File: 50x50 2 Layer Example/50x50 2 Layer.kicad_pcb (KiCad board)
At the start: 2 copper layers, 50 x 50 mm, 76 parts, among them J1 Conn_01x02, J2 Conn_01x02, J3 USB_C_Receptacle_USB2.0_14P, J4 Conn_01x03, J5 Conn_01x04, SW1 SW_SPST, SW2 Reset, U1 RP2040, U2 W25Q128JVPIQ TR, U3 Voltage Regulator, Y1 12MHz

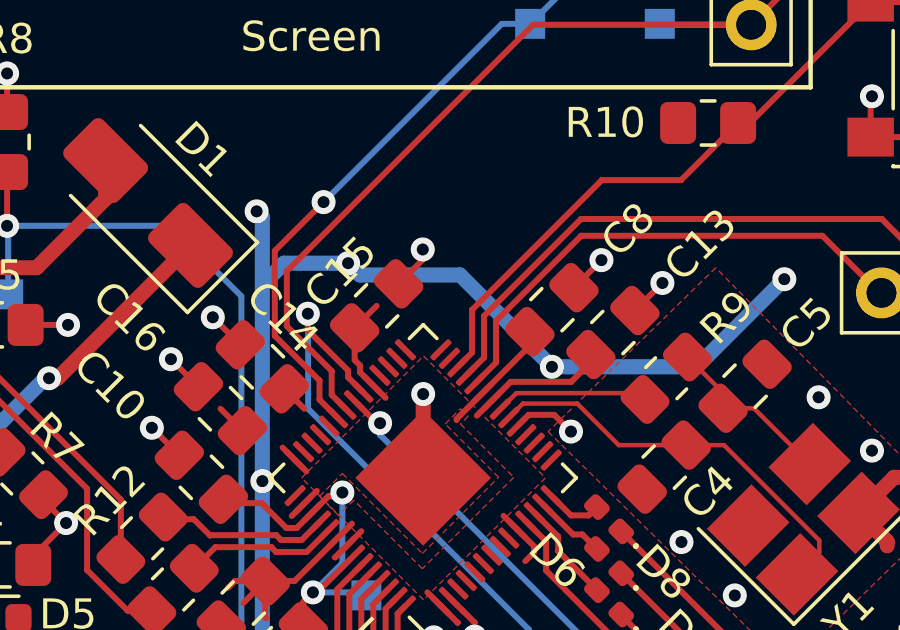
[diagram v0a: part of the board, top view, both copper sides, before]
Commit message: Rework power input switching and protection
- Replace diode-OR with DPDT source select (VBUS/battery) plus
  separate on/off switch
- Add SMAJ8.5A TVS on the battery input
- Add per-source indicator LEDs, 820R battery / 560R USB
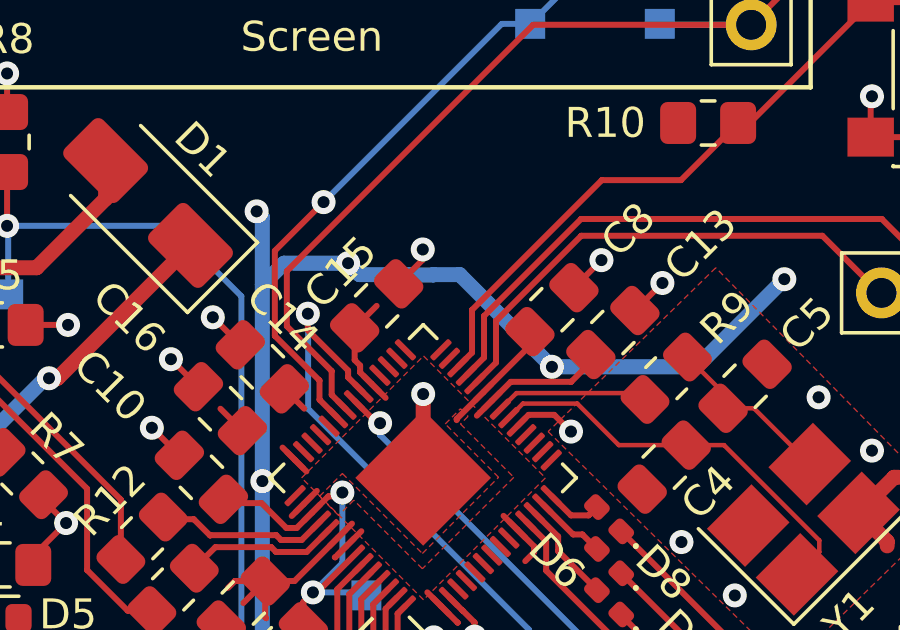
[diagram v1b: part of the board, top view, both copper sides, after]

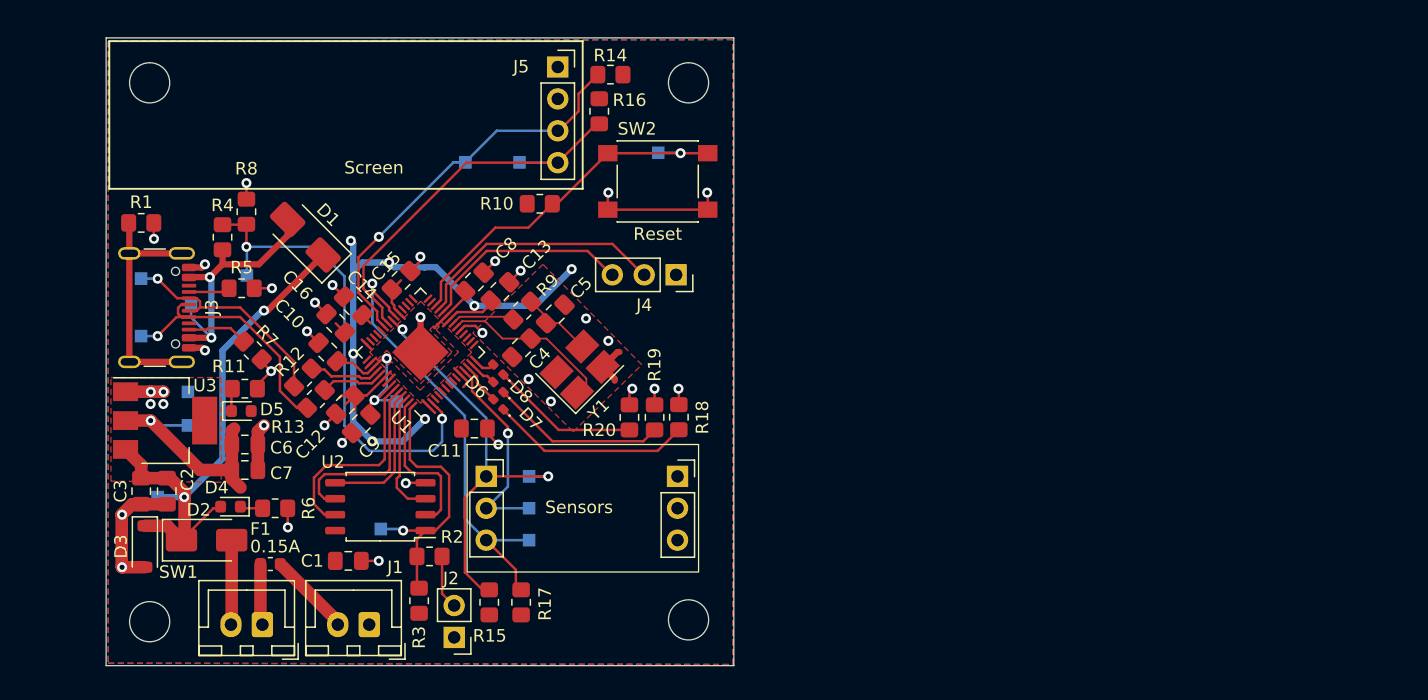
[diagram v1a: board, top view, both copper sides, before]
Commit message: Added Footprint for new Switches Attached LCSC numbers to components Started Cost Optimisation
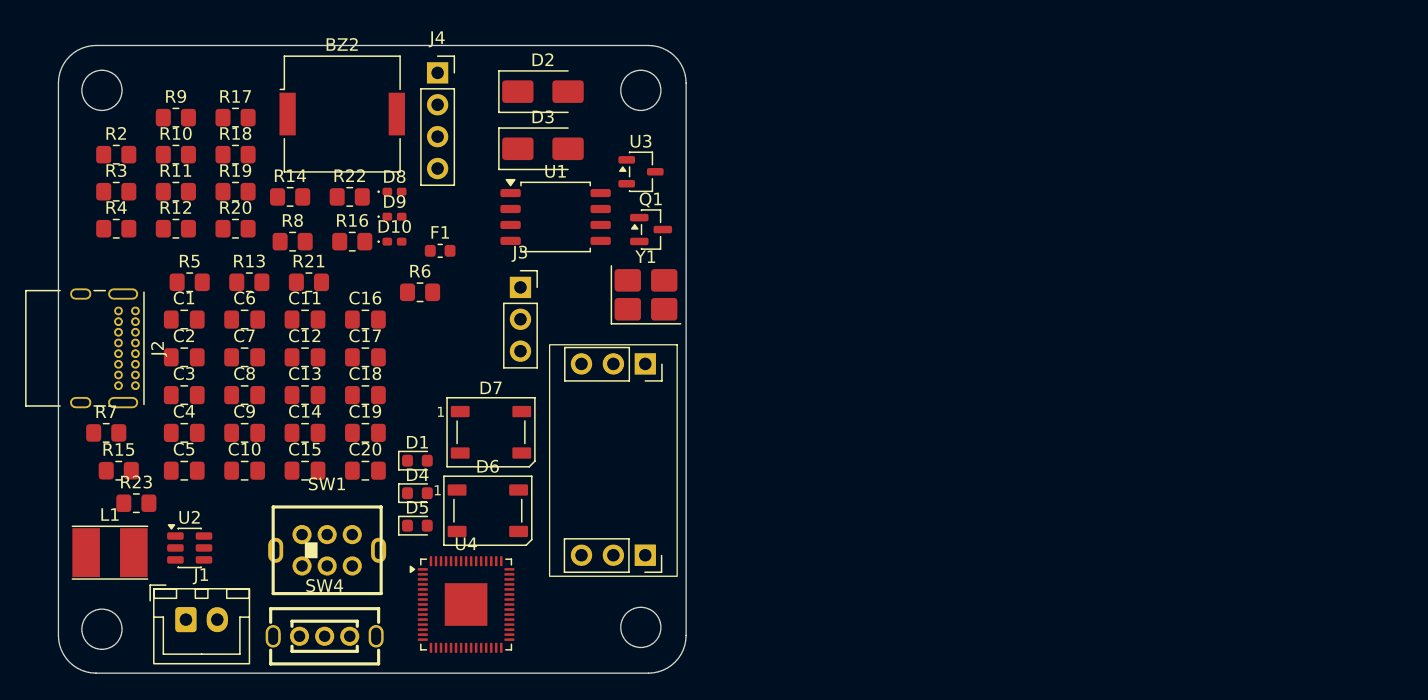
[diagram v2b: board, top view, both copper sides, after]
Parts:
- removed J5: Conn_01x04, Connector_PinSocket_2.54mm:PinSocket_1x04_P2.54mm_Vertical
- removed R1: 0R, Resistor_SMD:R_0805_2012Metric_Pad1.20x1.40mm_HandSolder
- removed SW2: Reset, Button_Switch_SMD:SW_SPST_PTS645
- removed TP1: GND, TestPoint:TestPoint_Pad_1.0x1.0mm
- removed TP10: 1V1, TestPoint:TestPoint_Pad_1.0x1.0mm
- removed TP11: INT_1, TestPoint:TestPoint_Pad_1.0x1.0mm
- removed TP12: I2C0_SCL, TestPoint:TestPoint_Pad_1.0x1.0mm
- removed TP13: I2C1_SCL, TestPoint:TestPoint_Pad_1.0x1.0mm
- removed TP14: I2C0_SDA, TestPoint:TestPoint_Pad_1.0x1.0mm
- removed TP15: I2C1_SDA, TestPoint:TestPoint_Pad_1.0x1.0mm
- removed TP2: VBUS, TestPoint:TestPoint_Pad_1.0x1.0mm
- removed TP3: D-, TestPoint:TestPoint_Pad_1.0x1.0mm
- removed TP4: D+, TestPoint:TestPoint_Pad_1.0x1.0mm
- removed TP5: USB_BOOT, TestPoint:TestPoint_Pad_1.0x1.0mm
- removed TP6: USB_DET, TestPoint:TestPoint_Pad_1.0x1.0mm
- removed TP7: BATT, TestPoint:TestPoint_Pad_1.0x1.0mm
- removed TP8: 3V3, TestPoint:TestPoint_Pad_1.0x1.0mm
- removed TP9: RST, TestPoint:TestPoint_Pad_1.0x1.0mm
- added BZ2: Buzzer, Buzzer_Beeper:Buzzer_Murata_PKMCS0909E, F.Cu at (97.0, 43.4)
- added C17: 100n, Capacitor_SMD:C_0805_2012Metric_Pad1.18x1.45mm_HandSolder, F.Cu at (98.8, 62.8)
- added C18: 100n, Capacitor_SMD:C_0805_2012Metric_Pad1.18x1.45mm_HandSolder, F.Cu at (98.8, 65.8)
- added C19: 100n, Capacitor_SMD:C_0805_2012Metric_Pad1.18x1.45mm_HandSolder, F.Cu at (98.8, 68.8)
- added C20: 10u, Capacitor_SMD:C_0805_2012Metric_Pad1.18x1.45mm_HandSolder, F.Cu at (98.8, 71.8)
- added D10: LED, LED_SMD:LED_0402_1005Metric_Pad0.77x0.64mm_HandSolder, F.Cu at (101.2, 53.6)
- added D9: LED, LED_SMD:LED_0402_1005Metric_Pad0.77x0.64mm_HandSolder, F.Cu at (101.2, 51.6)
- added L1: 3.3u, Inductor_SMD:L_Taiyo-Yuden_NR-40xx_HandSoldering, F.Cu at (78.5, 78.3)
- added Q1: MMBT3904, Package_TO_SOT_SMD:SOT-23, F.Cu at (121.6, 52.6)
- added R21: 80, Resistor_SMD:R_0805_2012Metric_Pad1.20x1.40mm_HandSolder, F.Cu at (94.3, 56.8)
- added R22: 80, Resistor_SMD:R_0805_2012Metric_Pad1.20x1.40mm_HandSolder, F.Cu at (97.6, 50.0)
- added R23: 80, Resistor_SMD:R_0805_2012Metric_Pad1.20x1.40mm_HandSolder, F.Cu at (80.6, 74.4)
- added SW4: ON_SW, Footprints:SW-TH_3P-L8.6-W4.5-P2.60, F.Cu at (95.6, 85.0)
- added U5: Sensor Board, Footprints:UCA_Sense, F.Cu at (118.6, 71.0)
- C1, C14, C15, C9: value 100nF -> 100n
- C10, C16: value 1uF -> 100n
- C11, C12, C13: value 100nF -> 4.7u
- C2: value 10uF -> 1u
- C3, C6: value 100nF -> 22u
- C4, C5: value 20pF -> 100n
- C7: value 10uF -> 15p
- C8: value 100nF -> 15p
- D1: value D_Schottky -> Blue LED; footprint Diode_SMD:D_SMA -> LED_SMD:LED_0603_1608Metric
- D3: value D_Zener -> SMAJ8.5A; footprint Diode_SMD:D_SOD-123 -> Diode_SMD:D_SMA
- D4: value Orange LED -> Green LED
- D6, D7: value LED -> WS2812B; footprint LED_SMD:LED_0402_1005Metric_Pad0.77x0.64mm_HandSolder -> LED_SMD:LED_WS2812B_PLCC4_5.0x5.0mm_P3.2mm
- F1: value 0.15A -> 0.25A
- J2: value Conn_01x02 -> USB_C_Receptacle_USB2.0_14P; footprint Connector_PinHeader_2.54mm:PinHeader_1x02_P2.54mm_Vertical -> Connector_USB:USB_C_Receptacle_GCT_USB4085
- J3: value USB_C_Receptacle_USB2.0_14P -> Conn_01x03; footprint Connector_USB:USB_C_Receptacle_GCT_USB4105-xx-A_16P_TopMnt_Horizontal -> Connector_PinSocket_2.54mm:PinSocket_1x03_P2.54mm_Vertical
- J4: value Conn_01x03 -> Conn_01x04; footprint Connector_PinSocket_2.54mm:PinSocket_1x03_P2.54mm_Vertical -> Connector_PinSocket_2.54mm:PinSocket_1x04_P2.54mm_Vertical
- R10: value 10k -> 1k
- R11: value 360R -> 360
- R12: value 27.4 -> 33
- R13: value 27.4 -> 27
- R14: value 4K7 -> 27
- R15, R16: value 4K7 -> 1k
- R18, R19, R20: value 130 -> 4K7
- R2: value 1k -> 820
- R3: value DNP -> 5k1
- R4: value 5.6k -> 560
- R5: value 5.1k -> 5k6
- R6: value 470R -> 5k1
- R7: value 5.1k -> 10k
- SW1: value SW_SPST -> PWR_SELECT; footprint Connector_JST:JST_XH_B2B-XH-A_1x02_P2.50mm_Vertical -> Footprints:SW-TH_KH-SS22D07-VG4H
- U1: value RP2040 -> W25Q32JVSSIQ; footprint Package_DFN_QFN:QFN-56-1EP_7x7mm_P0.4mm_EP3.2x3.2mm -> Package_SO:SOIC-8_5.3x5.3mm_P1.27mm
- U2: value W25Q128JVPIQ TR -> USBLC6-2SC6; footprint Package_SO:SOIC-8_5.23x5.23mm_P1.27mm -> Package_TO_SOT_SMD:SOT-23-6
- U3: value Voltage Regulator -> Voltage Regulator (MCP1755S-3302E/DB); footprint Package_TO_SOT_SMD:SOT-223 -> Package_TO_SOT_SMD:SOT-23-3
- U4: value ~ -> RP2354A; footprint Sense Board:UCA_Sense -> Package_DFN_QFN:QFN-60-1EP_7x7mm_P0.4mm_EP3.4x3.4mm
- moved D3 44.8 mm to (113.0, 46.2), turned to 0 degrees
- moved R17 44.8 mm to (88.5, 43.7), turned to 0 degrees
- moved D2 44.7 mm to (113.0, 41.6)
- moved U3 42.8 mm to (120.8, 48.0)
- moved R18 41.0 mm to (88.5, 46.6), turned to 0 degrees
- moved R2 40.6 mm to (79.0, 46.6), turned to 0 degrees
- moved R3 40.5 mm to (79.0, 49.6), turned to 0 degrees
- moved R19 37.9 mm to (88.5, 49.6), turned to 0 degrees
- moved J2 36.3 mm to (80.5, 59.1), turned to -90 degrees
- moved R20 34.8 mm to (88.5, 52.5), turned to 0 degrees
- moved C5 32.1 mm to (84.4, 71.8), turned to 0 degrees
- moved R9 31.6 mm to (83.8, 43.7), turned to 0 degrees
- moved R15 31.3 mm to (79.2, 71.8), turned to 0 degrees
- moved J3 30.1 mm to (111.2, 57.2), turned to 0 degrees
- moved R10 29.3 mm to (83.8, 46.6), turned to 0 degrees
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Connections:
- C1 pad 1: GND -> +3V3
- C1 pad 2: +3V3 -> GND
- C10 pad 1: GND -> +3V3
- C10 pad 2: +1V1 -> GND
- C11 pad 1: +3V3 -> GND
- C11 pad 2: GND -> +3V3
- C12 pad 1: +3V3 -> GND
- C12 pad 2: GND -> +1V1
- C13 pad 1: +3V3 -> GND
- C13 pad 2: GND -> Net-(U4-VREG_AVDD)
- C15 pad 1: GND -> +3V3
- C15 pad 2: +3V3 -> GND
- C16 pad 1: GND -> +3V3
- C16 pad 2: +3V3 -> GND
- C2 pad 1: +BATT -> +3V3
- C3 pad 1: +BATT -> VOUT
- C4 pad 1: /XIN -> VOUT
- C5 pad 1: Net-(C5-Pad1) -> +3V3
- C7 pad 1: +3V3 -> /XIN
- C8 pad 1: +1V1 -> Net-(C8-Pad1)
- C9 pad 1: +1V1 -> +3V3
- D1 pad 1: +BATT -> Net-(D1-K)
- D1 pad 2: VBUS -> Net-(D1-A)
- D2 pad 1: +BATT -> Net-(D2-K)
- D3 pad 1: +BATT -> Net-(D2-K)
- D4 pad 2: +BATT -> Net-(D4-A)
- D6 pad 1: Net-(D6-K) -> +3V3
- D6 pad 2: /LED_RED -> Net-(D6-DOUT)
- D7 pad 1: Net-(D7-K) -> +3V3
- D7 pad 2: /LED_YELLOW -> unconnected-(D7-DOUT-Pad2)
- D8 pad 2: /LED_GREEN -> /LED_RED
- F1 pad 1: Net-(SW1-A) -> Net-(D2-A)
- J4 pad 2: /SWD -> +3V3
- J4 pad 3: /SWCLK -> /I2C0_SCL
- R10 pad 1: /RUN -> Net-(R10-Pad1)
- R10 pad 2: +3V3 -> GND
- R12 pad 1: D- -> +3V3
- R12 pad 2: /USB_D- -> Net-(U4-VREG_AVDD)
- R13 pad 1: D+ -> D-
- R13 pad 2: /USB_D+ -> /USB_D-
- R14 pad 1: I2C0_SCL -> D+
- R14 pad 2: +3V3 -> /USB_D+
- R15 pad 1: I2C1_SCL -> Net-(Q1-B)
- R15 pad 2: +3V3 -> /BUZZER
- R16 pad 1: I2C0_SDA -> +3V3
- R16 pad 2: +3V3 -> Net-(BZ2--)
- R17 pad 1: I2C1_SDA -> /I2C0_SCL
- R18 pad 1: Net-(D6-K) -> /I2C1_SCL
- R18 pad 2: GND -> +3V3
- R19 pad 1: Net-(D7-K) -> /I2C0_SDA
- R19 pad 2: GND -> +3V3
- R2 pad 1: Net-(J2-Pin_2) -> Net-(D1-K)
- R2 pad 2: /QSPI_SS -> GND
- R20 pad 1: Net-(D8-K) -> /I2C1_SDA
- R20 pad 2: GND -> +3V3
- R3 pad 1: +3V3 -> Net-(J2-CC1)
- R3 pad 2: /QSPI_SS -> GND
- R4 pad 1: VBUS -> Net-(D4-K)
- R4 pad 2: USB_DET -> GND
- R5 pad 1: Net-(J3-CC1) -> VBUS
- R5 pad 2: GND -> USB_DET
- R6 pad 1: Net-(D4-K) -> GND
- R6 pad 2: GND -> Net-(J2-CC2)
- R7 pad 1: GND -> /SPI1_CSn
- R7 pad 2: Net-(J3-CC2) -> +3V3
- R9 pad 1: /Xout -> /XOUT
- R9 pad 2: Net-(C5-Pad1) -> Net-(C8-Pad1)
- SW1 pad 1: Net-(SW1-A) -> Net-(D2-K)
- SW1 pad 2: Net-(D2-A) -> Net-(SW1A-B)
- U1 pad 1: +3V3 -> /SPI1_CSn
- U1 pad 2: USB_DET -> /SPI1_MISO
- U1 pad 3: /GPIO_1 -> +3V3
- U1 pad 4: /GPIO_2 -> GND
- U1 pad 5: /GPIO_3 -> /SPI1_MOSI
- U1 pad 6: /GPIO_4 -> /SPI1_SCK
- U1 pad 7: /GPIO_5 -> +3V3
- U1 pad 8: /GPIO_6 -> +3V3
- U2 pad 1: /QSPI_SS -> Net-(J2-D--PadA7)
- U2 pad 2: /QSPI_SD1 -> GND
- U2 pad 3: /QSPI_SD2 -> Net-(J2-D+-PadA6)
- U2 pad 4: GND -> D+
- U2 pad 5: /QSPI_SD0 -> VBUS
- U2 pad 6: /QSPI_SCLK -> D-
- U3 pad 3: +BATT -> VOUT
- U4 pad 1: I2C1_SCL -> +3V3
- U4 pad 2: INT_1 -> USB_DET
- U4 pad 3: I2C1_SDA -> /LED_RGB
- U4 pad 4: GND -> /BUZZER
- U4 pad 5: unconnected-(U4-Pad5) -> /GPIO_3
- Y1 pad 3: Net-(C5-Pad1) -> Net-(C8-Pad1)
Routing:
- net +3V3: track 85.1 -> 0.00 mm, vias 8 -> 0
- net GND: track 66.6 -> 0.00 mm, vias 36 -> 0
- net +BATT: track 44.5 -> 0.00 mm, vias 2 -> 0
- net USB_DET: track 39.1 -> 0.00 mm, vias 2 -> 0
- net I2C1_SDA: track 36.1 -> 0.00 mm, vias 1 -> 0
- net I2C1_SCL: track 32.6 -> 0.00 mm, vias 2 -> 0
- net I2C0_SCL: track 32.3 -> 0.00 mm, vias 1 -> 0
- net I2C0_SDA: track 31.9 -> 0.00 mm
- net /RUN: track 29.4 -> 0.00 mm, vias 1 -> 0
- net /QSPI_SS: track 22.2 -> 0.00 mm, vias 1 -> 0
- net VBUS: track 21.5 -> 0.00 mm, vias 2 -> 0
- net D+: track 21.2 -> 0.00 mm, vias 1 -> 0
- net /SWD: track 20.3 -> 0.00 mm
- net Net-(J3-SHIELD): track 19.5 -> 0.00 mm
- net D-: track 18.6 -> 0.00 mm, vias 1 -> 0
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- removed copper zone on F.Cu, net +1V1
- removed copper zone on F.Cu, net +3V3
- removed copper zone on B.Cu, net GND
- removed copper zone on F.Cu, net GND
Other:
- outline, holes or cut-outs redrawn
- board text removed: "12/04/24"
- board text removed: "By Grayson Fenemor"
- board text removed: "Power Management"
- board text removed: "REV: B"
- board text removed: "RP2040 MCU"
- board text removed: "Screen"
- board text removed: "Sensors"
- board text removed: "UC Aerospace"
- board text removed: "USB C"

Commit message: Updated Inductor
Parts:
- C1, C10, C11, C12, C13, C14, C15, C16, C17, C18, C19, C2, C3, C4, C5, C6, C7, C8, C9: footprint Capacitor_SMD:C_0805_2012Metric_Pad1.18x1.45mm_HandSolder -> Capacitor_SMD:C_0603_1608Metric_Pad1.08x0.95mm_HandSolder
- D1, D4, D5: footprint LED_SMD:LED_0603_1608Metric -> LED_SMD:LED_0805_2012Metric_Pad1.15x1.40mm_HandSolder
- R10, R11, R12, R13, R14, R15, R16, R17, R18, R19, R2, R20, R21, R22, R23, R4, R5, R9: footprint Resistor_SMD:R_0805_2012Metric_Pad1.20x1.40mm_HandSolder -> Capacitor_SMD:C_0603_1608Metric_Pad1.08x0.95mm_HandSolder
- R3, R6, R7, R8: footprint Resistor_SMD:R_0805_2012Metric_Pad1.20x1.40mm_HandSolder -> Resistor_SMD:R_0603_1608Metric
- moved R22 0.80 mm to (96.8, 50.0)

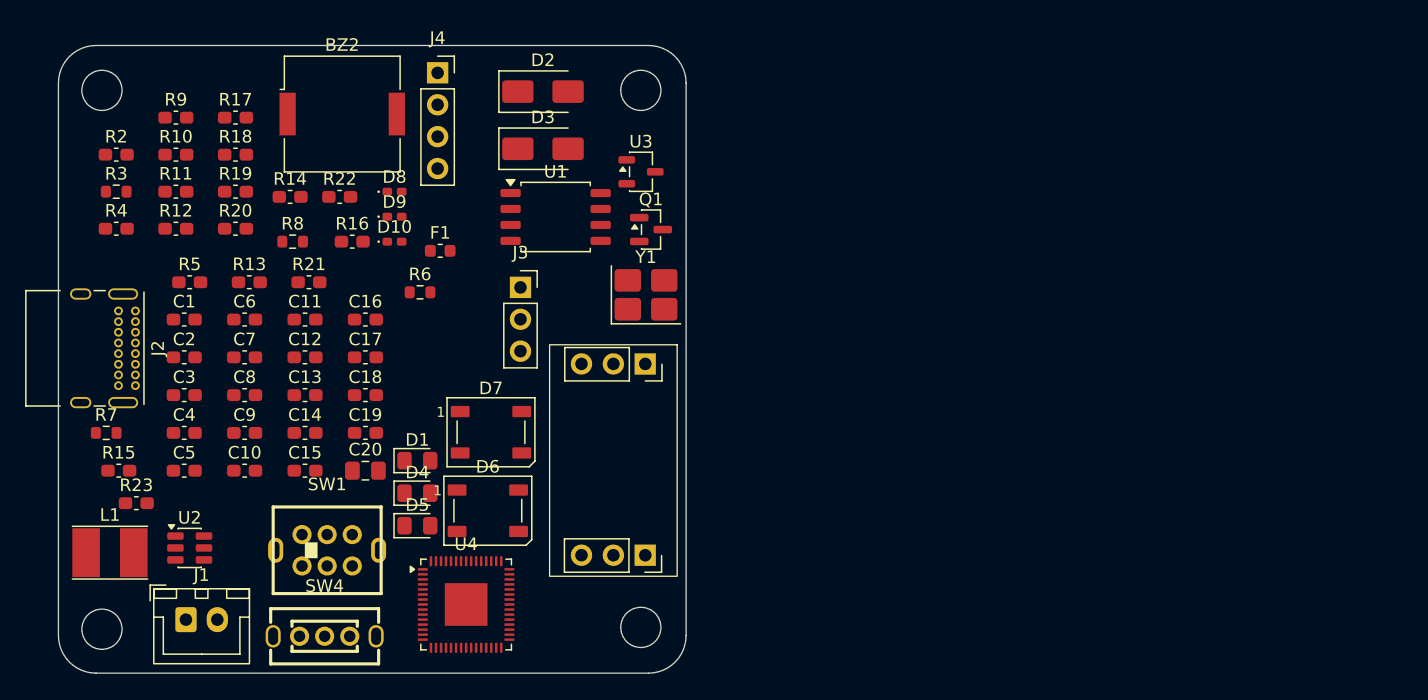
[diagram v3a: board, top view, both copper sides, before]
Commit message: Fixed RP2354A Schematic Added LCSC Part Numbers Added Datasheets
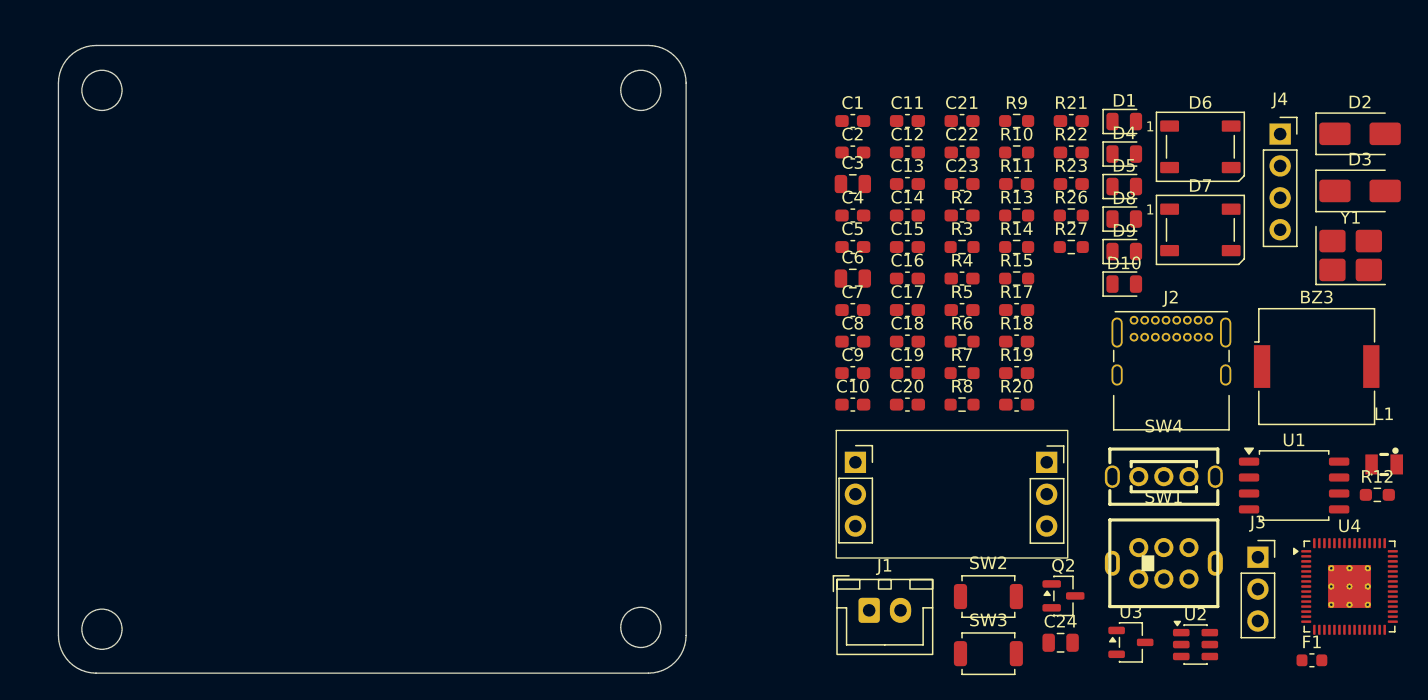
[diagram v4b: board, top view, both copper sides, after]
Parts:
- removed BZ2: Buzzer, Buzzer_Beeper:Buzzer_Murata_PKMCS0909E
- removed Q1: MMBT3904, Package_TO_SOT_SMD:SOT-23
- removed R16: 1k, Capacitor_SMD:C_0603_1608Metric_Pad1.08x0.95mm_HandSolder
- added BZ3: Buzzer, Buzzer_Beeper:Buzzer_Murata_PKMCS0909E, F.Cu at (174.6, 63.5)
- added C21: 100n, Capacitor_SMD:C_0603_1608Metric_Pad1.08x0.95mm_HandSolder, F.Cu at (146.4, 44.0)
- added C22: 100n, Capacitor_SMD:C_0603_1608Metric_Pad1.08x0.95mm_HandSolder, F.Cu at (146.4, 46.5)
- added C23: 100n, Capacitor_SMD:C_0603_1608Metric_Pad1.08x0.95mm_HandSolder, F.Cu at (146.4, 49.0)
- added C24: 10u, Capacitor_SMD:C_0805_2012Metric, F.Cu at (154.2, 85.5)
- added Q2: MMBT3904, Package_TO_SOT_SMD:SOT-23, F.Cu at (154.5, 81.8)
- added R26: 1k, Resistor_SMD:R_0603_1608Metric_Pad0.98x0.95mm_HandSolder, F.Cu at (155.1, 51.5)
- added R27: 1k, Resistor_SMD:R_0603_1608Metric_Pad0.98x0.95mm_HandSolder, F.Cu at (155.1, 54.0)
- added SW2: SW_Push, Button_Switch_SMD:SW_SPST_TS-1088-xR020, F.Cu at (148.5, 81.8)
- added SW3: SW_Push, Button_Switch_SMD:SW_SPST_TS-1088-xR020, F.Cu at (148.5, 86.4)
- C13: value 4.7u -> 100n
- C14, C15: value 100n -> 4.7u
- C20: value 10u -> 100n; footprint Capacitor_SMD:C_0805_2012Metric_Pad1.18x1.45mm_HandSolder -> Capacitor_SMD:C_0603_1608Metric_Pad1.08x0.95mm_HandSolder
- C3, C6: footprint Capacitor_SMD:C_0603_1608Metric_Pad1.08x0.95mm_HandSolder -> Capacitor_SMD:C_0805_2012Metric
- D1: value Blue LED -> Yellow LED; footprint LED_SMD:LED_0805_2012Metric_Pad1.15x1.40mm_HandSolder -> LED_SMD:LED_0805_2012Metric
- D10: value LED -> Green LED; footprint LED_SMD:LED_0402_1005Metric_Pad0.77x0.64mm_HandSolder -> LED_SMD:LED_0805_2012Metric
- D4, D5: footprint LED_SMD:LED_0805_2012Metric_Pad1.15x1.40mm_HandSolder -> LED_SMD:LED_0805_2012Metric
- D8: value LED -> Red LED; footprint LED_SMD:LED_0402_1005Metric_Pad0.77x0.64mm_HandSolder -> LED_SMD:LED_0805_2012Metric
- D9: value LED -> Yellow LED; footprint LED_SMD:LED_0402_1005Metric_Pad0.77x0.64mm_HandSolder -> LED_SMD:LED_0805_2012Metric
- L1: footprint Inductor_SMD:L_Taiyo-Yuden_NR-40xx_HandSoldering -> Footprints:IND-SMD_L2.0-W1.6_AOTA-B201610S3R3-101-T
- R10, R12, R14, R9: footprint Capacitor_SMD:C_0603_1608Metric_Pad1.08x0.95mm_HandSolder -> Resistor_SMD:R_0603_1608Metric_Pad0.98x0.95mm_HandSolder
- R11: value 360 -> 390
- R13: value 27 -> 1k; footprint Capacitor_SMD:C_0603_1608Metric_Pad1.08x0.95mm_HandSolder -> Resistor_SMD:R_0603_1608Metric_Pad0.98x0.95mm_HandSolder
- R15: value 1k -> 27; footprint Capacitor_SMD:C_0603_1608Metric_Pad1.08x0.95mm_HandSolder -> Resistor_SMD:R_0603_1608Metric_Pad0.98x0.95mm_HandSolder
- R21, R22, R23: value 80 -> 100
- R3, R6, R7, R8: footprint Resistor_SMD:R_0603_1608Metric -> Resistor_SMD:R_0603_1608Metric_Pad0.98x0.95mm_HandSolder
- U4: value RP2354A -> RP2354_60QFN; footprint Package_DFN_QFN:QFN-60-1EP_7x7mm_P0.4mm_EP3.4x3.4mm -> Package_DFN_QFN:QFN-60-1EP_7x7mm_P0.4mm_EP3.4x3.4mm_ThermalVias
- moved L1 101.7 mm to (180.0, 71.3)
- moved R12 98.0 mm to (179.5, 73.7)
- moved U2 80.5 mm to (165.0, 85.7)
- moved J2 79.5 mm to (160.1, 59.8), turned to 0 degrees
- moved R23 78.7 mm to (155.1, 49.0)
- moved F1 76.7 mm to (174.2, 86.9)
- moved R15 73.1 mm to (150.7, 56.5)
- moved U4 70.4 mm to (177.2, 81.0)
- moved R7 68.3 mm to (146.4, 64.0)
- moved SW4 68.0 mm to (162.4, 72.3)
- moved R2 67.5 mm to (146.4, 51.5)
- moved R3 67.5 mm to (146.4, 54.0)
- moved R4 67.5 mm to (146.4, 56.5)
- moved J4 67.3 mm to (171.7, 45.0)
- moved R11 67.0 mm to (150.7, 49.0)
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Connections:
- net Net-(U4-VREG_LX) renamed /VREG_LX
- C11 pad 1: GND -> +3V3
- C11 pad 2: +3V3 -> GND
- C12 pad 1: GND -> +1V1
- C12 pad 2: +1V1 -> GND
- C13 pad 1: GND -> +1V1
- C13 pad 2: Net-(U4-VREG_AVDD) -> GND
- C14 pad 1: +3V3 -> /VREG_AVDD
- C15 pad 1: +3V3 -> +1V1
- C16 pad 1: +3V3 -> +1V1
- C20 pad 1: GND -> +3V3
- C20 pad 2: +3V3 -> GND
- R12 pad 2: Net-(U4-VREG_AVDD) -> /VREG_AVDD
- R13 pad 1: D- -> /QSPI_SS
- R13 pad 2: /USB_D- -> /~{USB_BOOT}
- R14 pad 1: D+ -> /USB_D+
- R14 pad 2: /USB_D+ -> Net-(U4-USB_DP)
- R15 pad 1: Net-(Q1-B) -> /USB_D-
- R15 pad 2: /BUZZER -> Net-(U4-USB_DM)
- SW1 pad 7: (no net) -> unconnected-(SW1A-C-Pad7)
- SW1 pad 8: (no net) -> unconnected-(SW1A-C-Pad8)
- SW4 pad 4: (no net) -> unconnected-(SW4-C-Pad4)
- SW4 pad 5: (no net) -> unconnected-(SW4-C-Pad5)
- U4 pad 11: Net-(U4-IOVDD-Pad11) -> +3V3
- U4 pad 20: Net-(U4-IOVDD-Pad11) -> +3V3
- U4 pad 23: Net-(U4-DVDD-Pad23) -> +1V1
- U4 pad 30: Net-(U4-IOVDD-Pad11) -> +3V3
- U4 pad 38: Net-(U4-IOVDD-Pad11) -> +3V3
- U4 pad 39: Net-(U4-DVDD-Pad23) -> +1V1
- U4 pad 45: Net-(U4-IOVDD-Pad11) -> +3V3
- U4 pad 46: Net-(U4-VREG_AVDD) -> /VREG_AVDD
- U4 pad 51: /USB_D- -> Net-(U4-USB_DM)
- U4 pad 52: /USB_D+ -> Net-(U4-USB_DP)
- U4 pad 6: +3V3 -> +1V1
- U4 pad 60: unconnected-(U4-~{QSPI_SS}-Pad60) -> /QSPI_SS
